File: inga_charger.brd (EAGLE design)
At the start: 25.4 x 14.9 mm, 10 parts

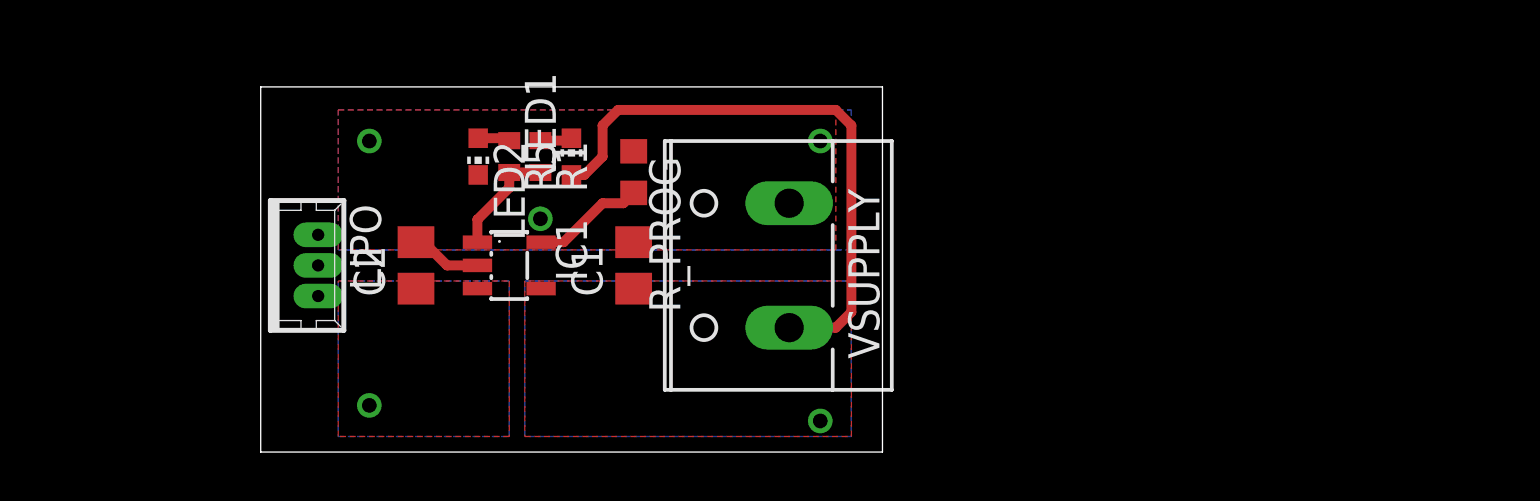
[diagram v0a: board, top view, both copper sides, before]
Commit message: Adds new version of board and schematic
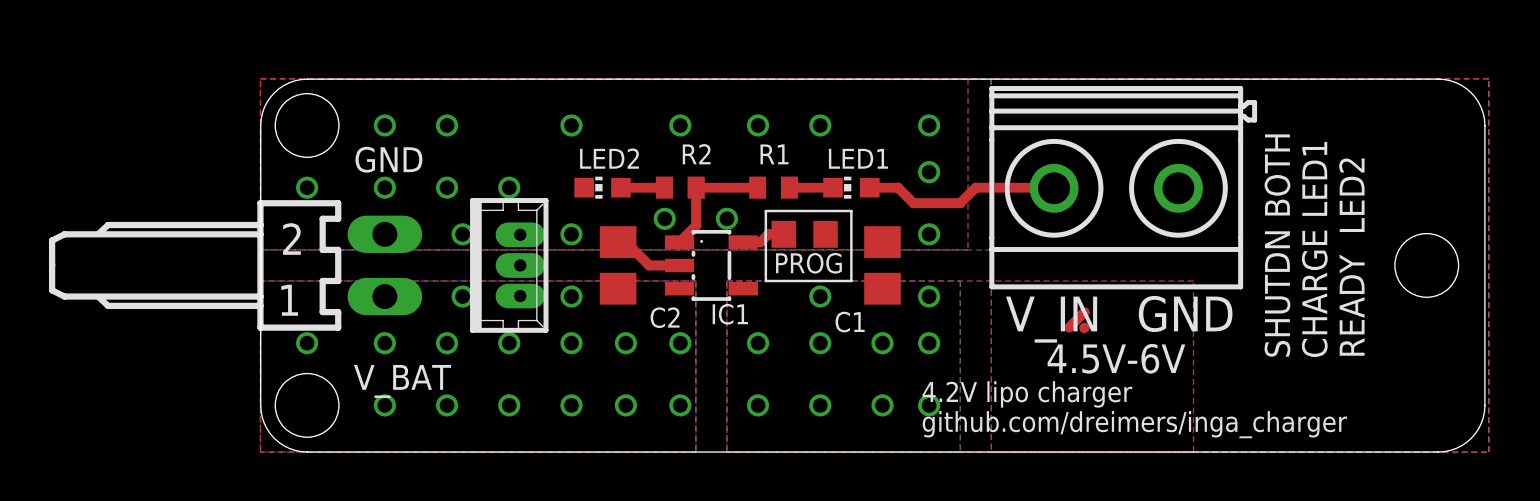
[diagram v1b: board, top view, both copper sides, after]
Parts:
- removed R5: 470, rcl:R0402
- added J1: 22-05-7028-02, con-molex:7395-02
- added R2: 470, rcl:R0402
- VSUPPLY: value (none) -> MKDSN1,5/2-5,08; device con-wago-508:W237-132 -> con-phoenix-508:MKDSN1,5/2-5,08
- moved VSUPPLY 14.3 mm to (34.9, 10.8), turned to 180 degrees
- moved LED1 11.5 mm to (24.1, 10.8), turned to 90 degrees
- moved C1 10.2 mm to (25.4, 7.62)
- moved R1 9.61 mm to (21.0, 10.8), turned to 180 degrees
- moved C2 8.26 mm to (14.6, 7.62)
- moved LIPO 8.26 mm to (10.2, 7.62)
- moved IC1 8.25 mm to (18.4, 7.62)
- moved R_PROG 7.43 mm to (22.2, 8.89), turned to 180 degrees
- moved LED2 5.24 mm to (14.0, 10.8), turned to 90 degrees
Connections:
- removed net VBAT: C2.1, IC1.3, LIPO.1
- removed net VDD: C1.1, IC1.4, LED1.A, VSUPPLY.1
- new net V_BAT: C2.1, IC1.3, J1.1, LIPO.1
- new net V_IN: C1.1, IC1.4, LED1.A, VSUPPLY.2
- net GND: now also J1.2, VSUPPLY.1; no longer VSUPPLY.2
- net N$2: now also R2.2; no longer R5.2
- net N$5: now also R2.1; no longer R5.1
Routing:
- net VDD: track 24.0 -> 0.00 mm, vias 1 -> 0
- net V_IN: track 0.00 -> 8.99 mm, vias 0 -> 10
- net N$4: track 4.61 -> 1.79 mm
- net GND: vias 3 -> 17
- added copper zone on layer 1, net V_BAT
- added copper zone on layer 16, net V_BAT
- added copper zone on layer 1, net V_IN
- added copper zone on layer 16, net V_IN
- removed copper zone on layer 1, net VBAT
- removed copper zone on layer 16, net VBAT
- removed copper zone on layer 1, net VDD
- removed copper zone on layer 16, net VDD
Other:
- board size 25.4 x 14.9 mm -> 50 x 15.2 mm
- board text added: "4.2V lipo charger github.com/dreimers/inga_charger"
- board text added: "4.5V-6V"
- board text added: "GND"
- board text added: "PROG"
- board text added: "SHUTDN BOTH CHARGE LED1 READY LED2"
- board text added: "V_BAT"
- board text added: "V_IN"
